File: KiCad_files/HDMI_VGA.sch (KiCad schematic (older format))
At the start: 52 parts, among them J7 TFP410, J8 DB15_Female_HighDensity_Mount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

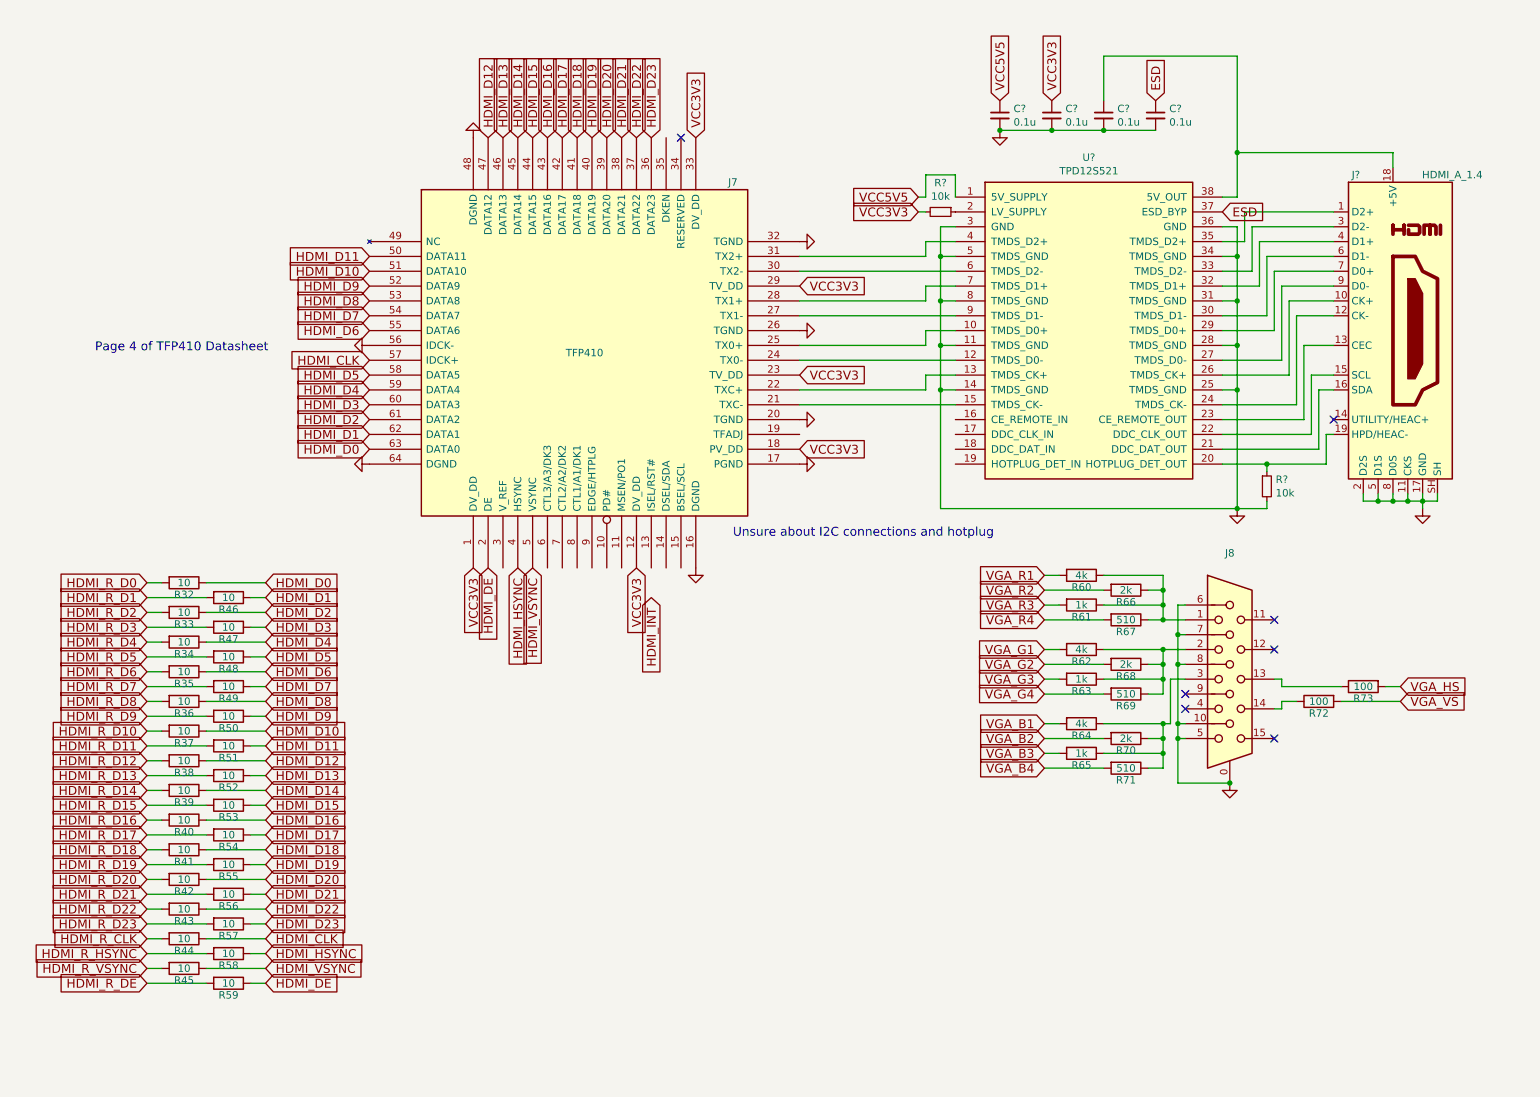
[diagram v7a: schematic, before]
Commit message: Finished HDMI. Added I2C
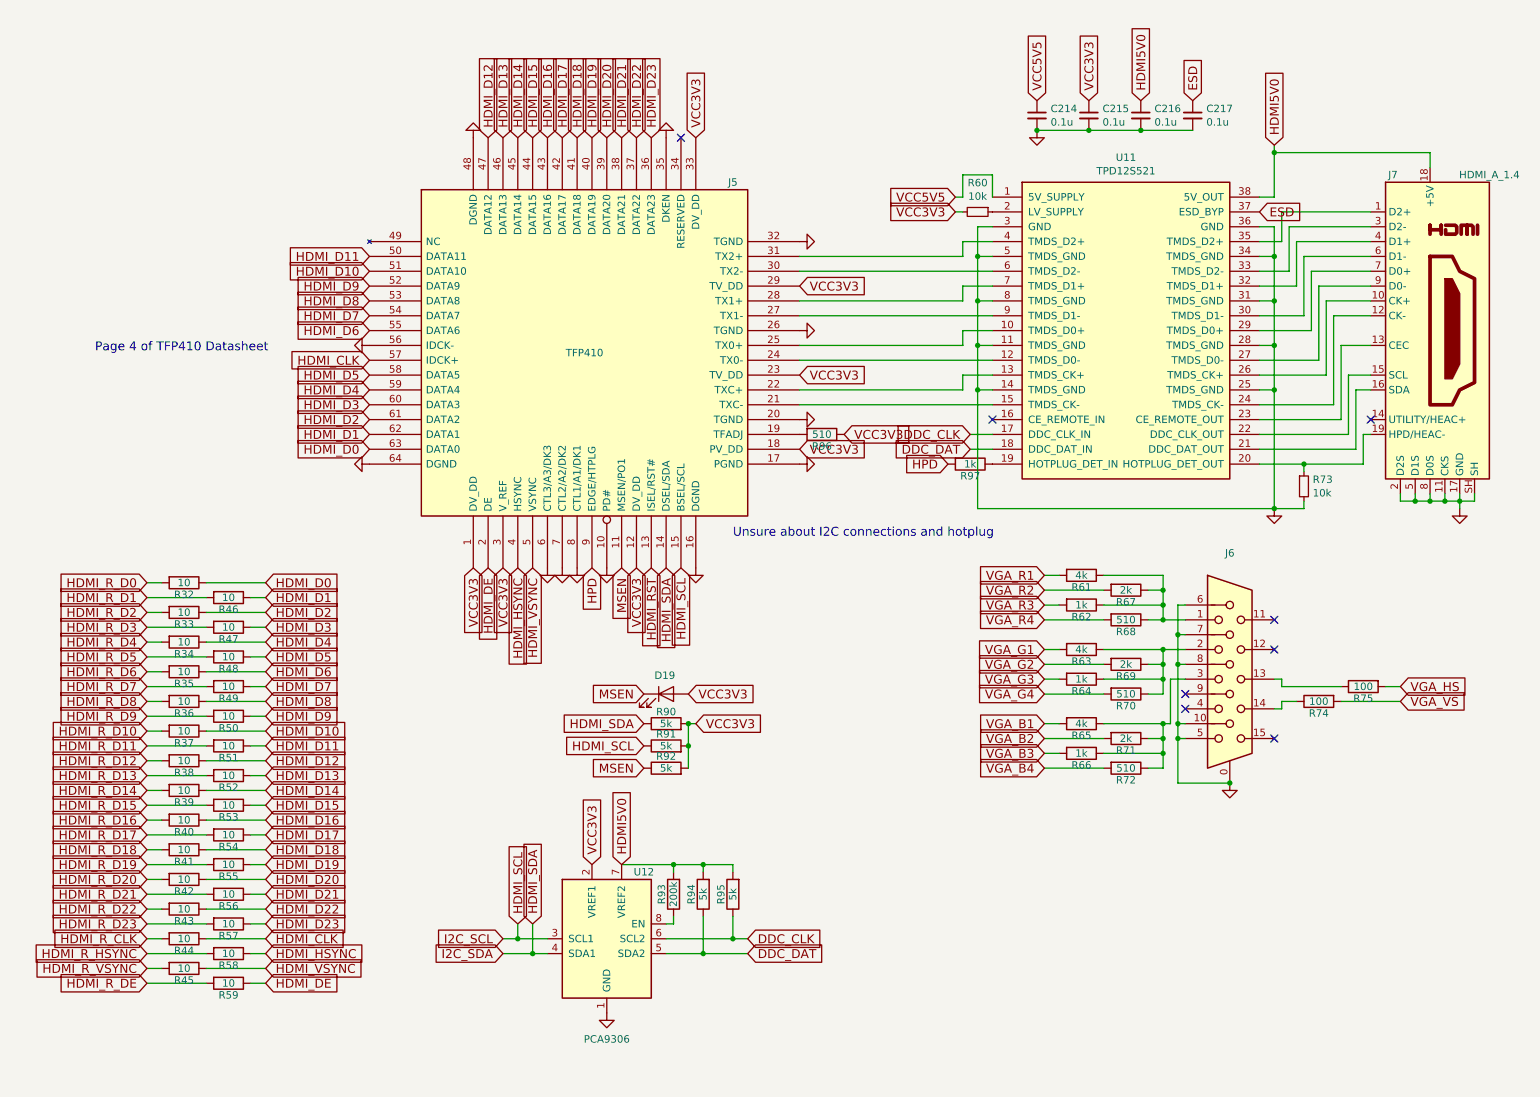
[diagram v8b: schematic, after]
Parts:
- added D19: LED, symbol Device:LED
- added R90, R91, R92, R94, R95: 5k, symbol Device:R
- added R93: 200k, symbol Device:R
- added R96: 510, symbol Device:R
- added R97: 1k, symbol Device:R
- added U12: PCA9306, symbol Interface:PCA9306
- gave numbers to parts that had none: 8
- renumbered J7 to J5, J8 to J6, R60 to R61, R61 to R62, R62 to R63, R63 to R64, R64 to R65, R65 to R66, R66 to R67, R67 to R68, R68 to R69, R69 to R70, R70 to R71, R71 to R72, R72 to R74, R73 to R75
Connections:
- net GND: now also J5.10 (PD#), J5.35 (DKEN), J5.6 (CTL3/A3/DK3), J5.7 (CTL2/A2/DK2), J5.8 (CTL1/A1/DK1), U12.1 (GND)
- net VCC3V3: now also J5.3 (V_REF), D19.2 (A), R90.2, R91.2, R92.2, R96.1, U12.2 (VREF1)
- net MSEN: now reaches J5.11 (MSEN/PO1)
- net MSEN: now also D19.1 (K), R92.1
- net HDMI_RST: now reaches J5.13 (ISEL/RST#)
- net HDMI_SDA: now reaches J5.14 (DSEL/SDA)
- net HDMI_SDA: now also R90.1, U12.4 (SDA1)
- net HDMI_SCL: now reaches J5.15 (BSEL/SCL)
- net HDMI_SCL: now also R91.1, U12.3 (SCL1)
- net at J5.19 (TFADJ): now also R96.2
- net HPD: now reaches J5.9 (EDGE/HTPLG)
- net HPD: now also R97.2
- net HDMI5V0: now reaches C216.1, J7.18 (+5V), U11.38 (5V_OUT)
- net HDMI5V0: now also R93.2, R94.2, R95.2, U12.7 (VREF2)
- net DDC_CLK: now reaches U11.17 (DDC_CLK_IN)
- net DDC_CLK: now also R95.1, U12.6 (SCL2)
- net DDC_DAT: now reaches U11.18 (DDC_DAT_IN)
- net DDC_DAT: now also R94.1, U12.5 (SDA2)
- net at U11.19 (HOTPLUG_DET_IN): now also R97.1
- new net: R93.1, U12.8 (EN)
- no-connect marks 7 -> 8
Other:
- moved on the sheet: C214, C215, C216, C217, J7, R60, R73, U11
